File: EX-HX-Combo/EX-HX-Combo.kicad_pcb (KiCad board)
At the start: 2 copper layers, 124.5 x 120.4 mm, 46 parts, among them CN1 DB9 Male, J1 IDE_CONNECTOR, J2 Bus_Tandy_Plus, J3 Bus_Tandy_Plus_Through, SW1 SW_DIP_x10, U1 BIOS FLASH, U2 74HCT245, U3 1.8432 MHz, U4 DS1315, U5 AS6C4008-55PCN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

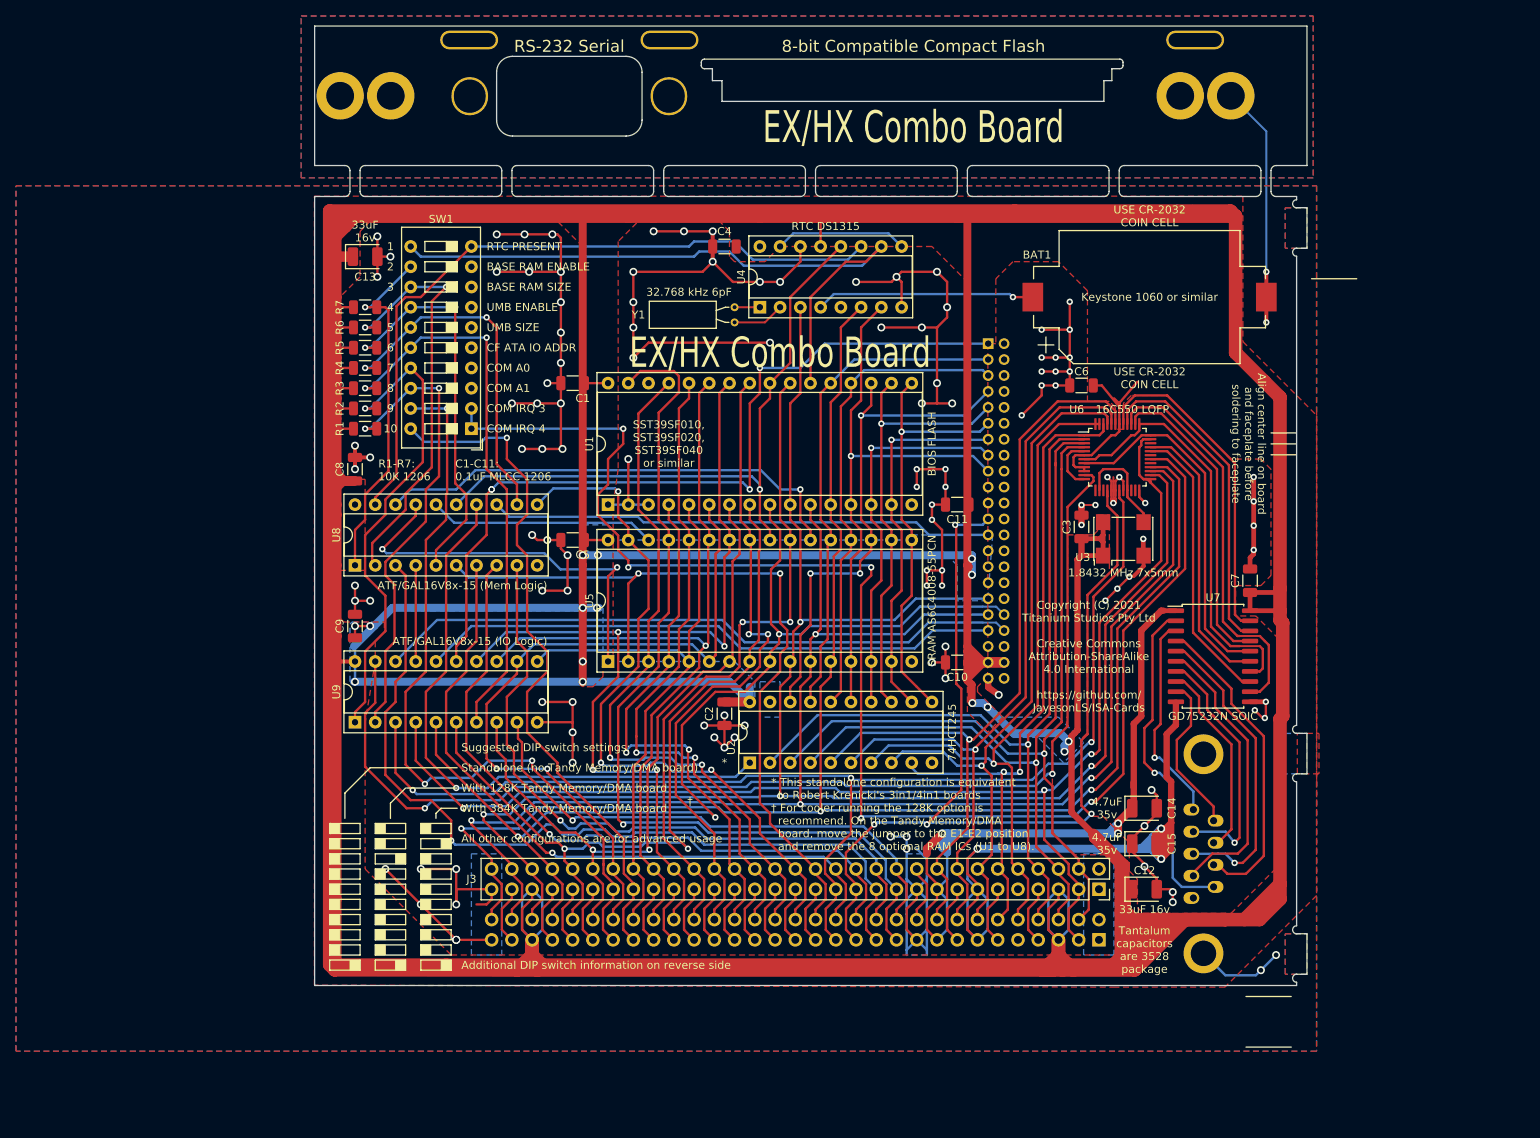
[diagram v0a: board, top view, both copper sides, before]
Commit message: EX-HX-Combo: Move backplate back to original position in prep for moving to new scene.
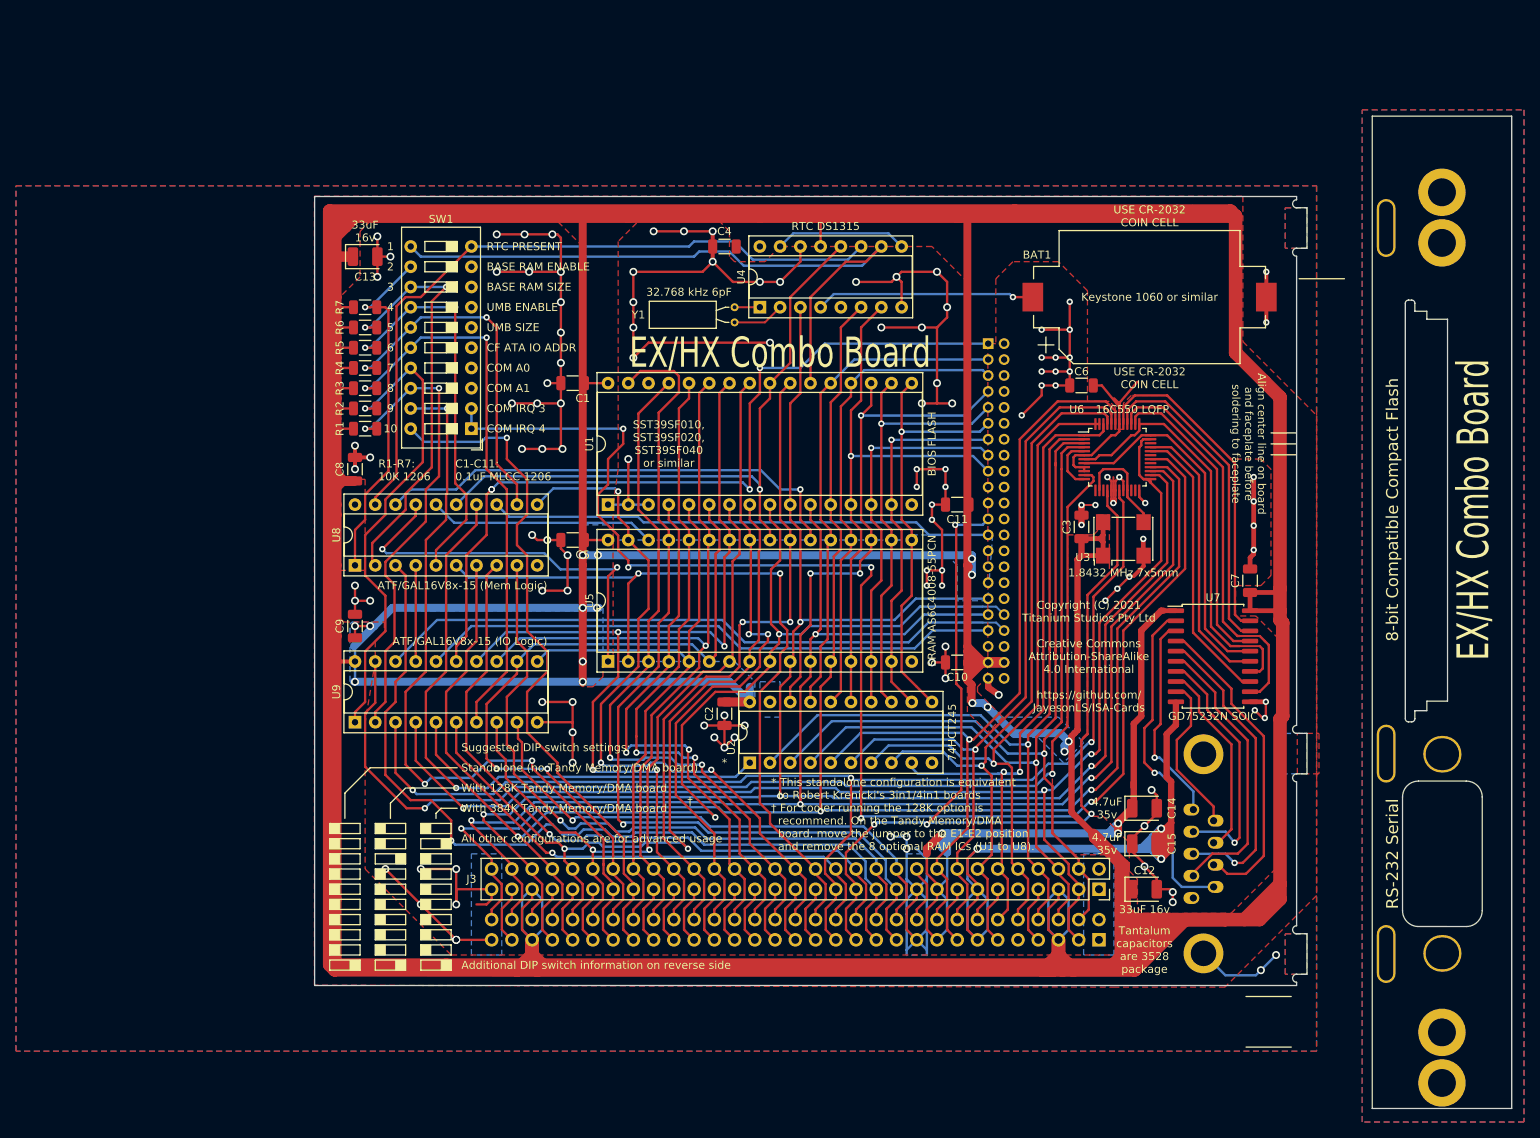
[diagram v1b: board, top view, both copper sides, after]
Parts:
- moved H4 185.6 mm to (261.5, 148.8), turned to 0 degrees
- moved H3 176.7 mm to (261.5, 142.4), turned to 0 degrees
- moved H5 162.5 mm to (254.5, 132.6), turned to 90 degrees
- moved H8 144.7 mm to (255.3, 120.0), turned to 270 degrees
- moved H6 126.9 mm to (254.5, 107.4), turned to 90 degrees
- moved H2 37.7 mm to (261.5, 43.4), turned to 0 degrees
- moved H7 33.6 mm to (254.5, 41.5), turned to 90 degrees
- moved H1 29.1 mm to (261.5, 37.0), turned to 0 degrees
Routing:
- net GND: track 497.0 -> 473.1 mm
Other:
- board size 124.5 x 120.4 mm -> 150.2 x 124.5 mm

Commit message: EX-HX-Combo: Initial work preparing for JLCPCB assembly. Other minor tweaks also.
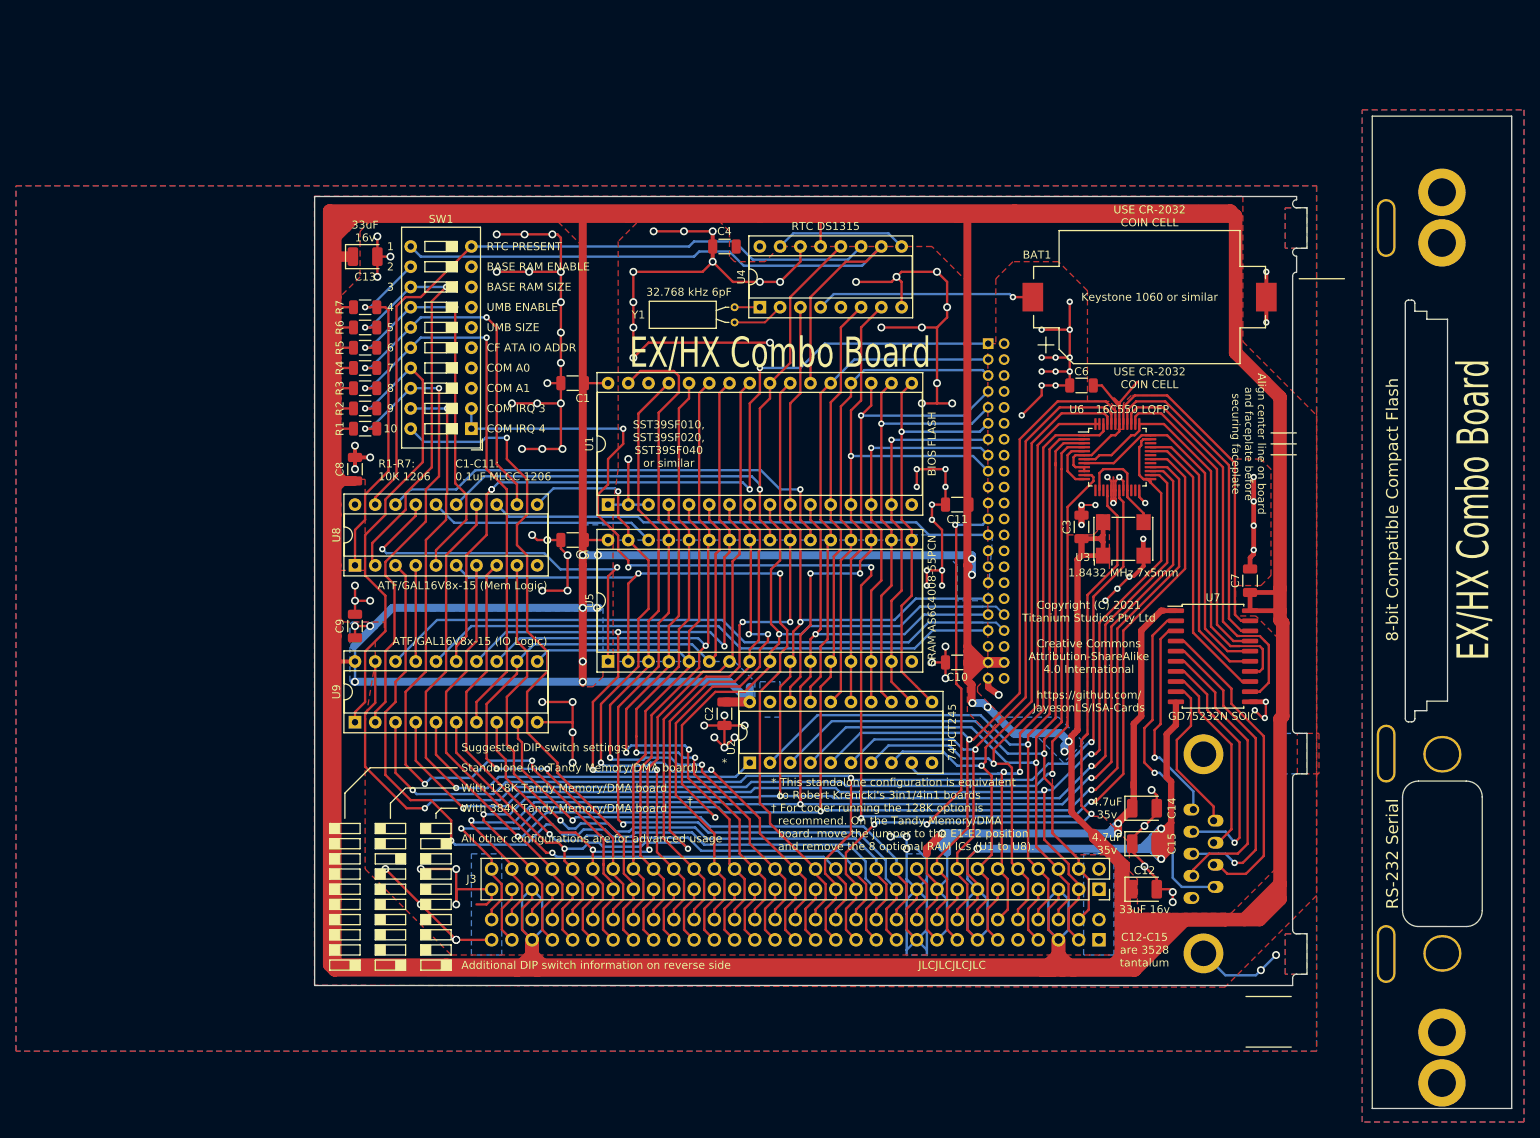
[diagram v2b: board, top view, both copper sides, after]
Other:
- outline, holes or cut-outs redrawn
- board text added: "Align center line on board and faceplate before securing faceplate"
- board text added: "C12-C15 are 3528 tantalum"
- board text added: "COM"
- board text added: "JLCJLCJLCJLC"
- board text added: "v1.01"
- board text removed: "Align center line on board and faceplate before soldering to faceplate"
- board text removed: "Serial"
- board text removed: "Tantalum capacitors are 3528 package"
- board text removed: "v1.0"

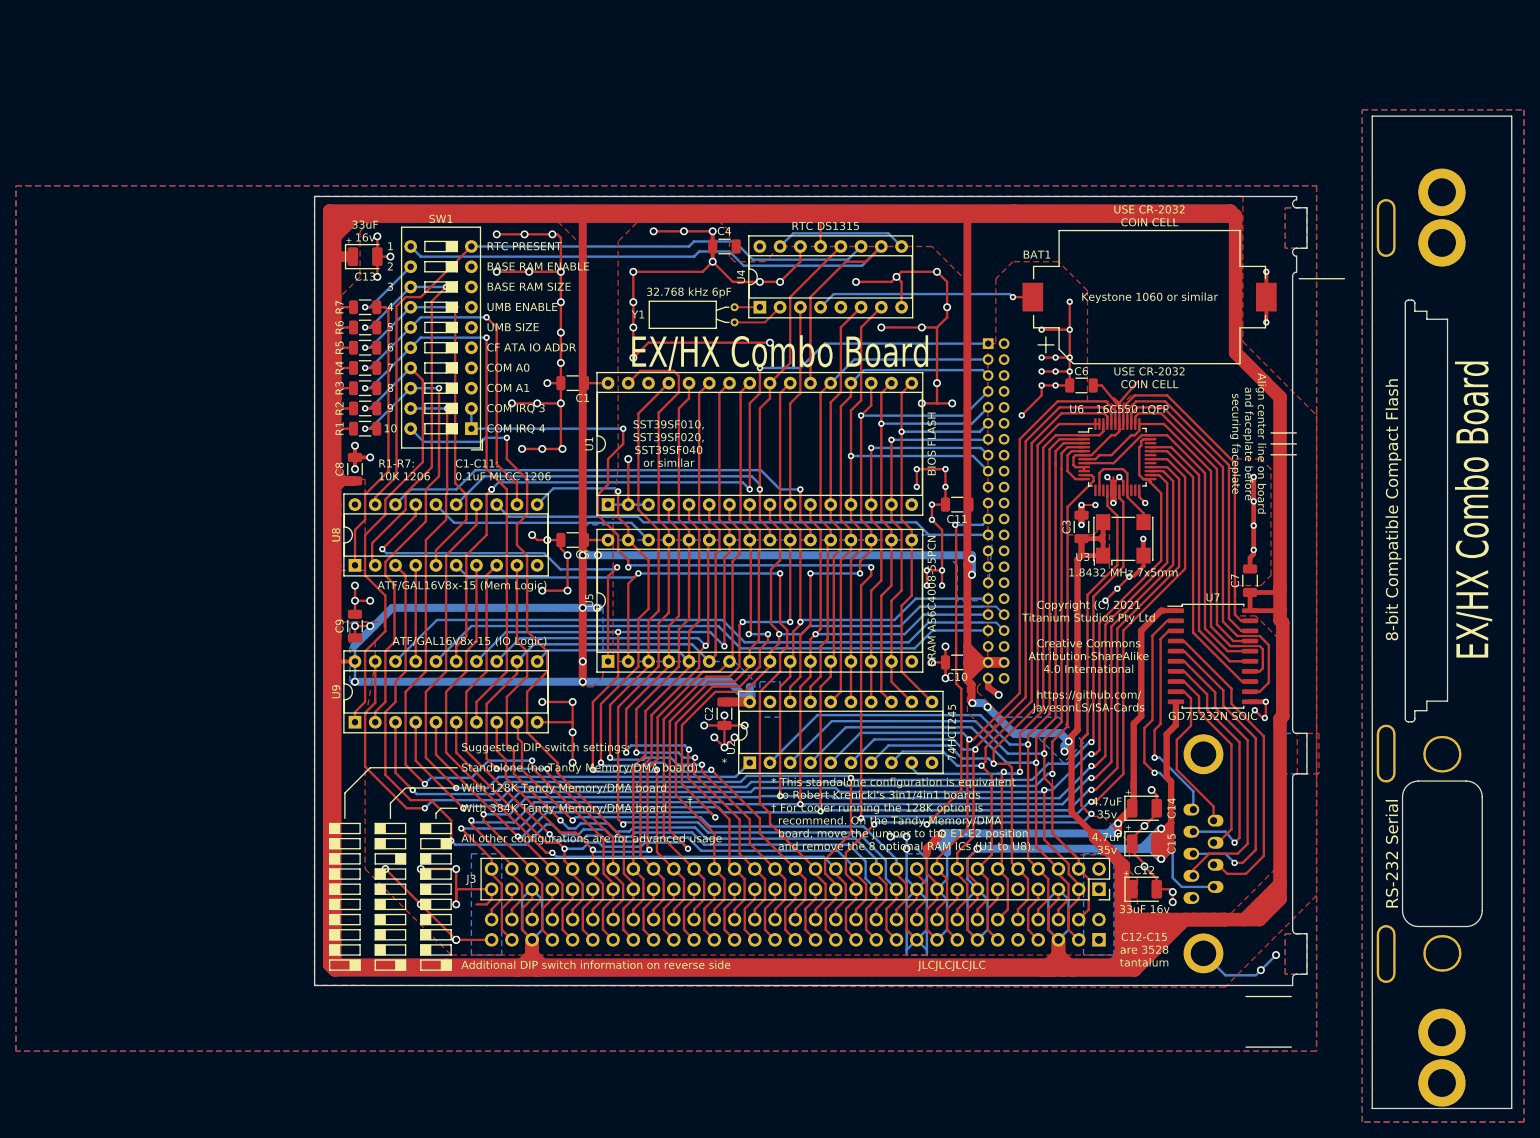
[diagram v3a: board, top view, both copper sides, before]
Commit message: Use correct DB-9 footprint on EX-HX-Combo. Also remove ground from alighment pins and space out the resitors in the top left bank.
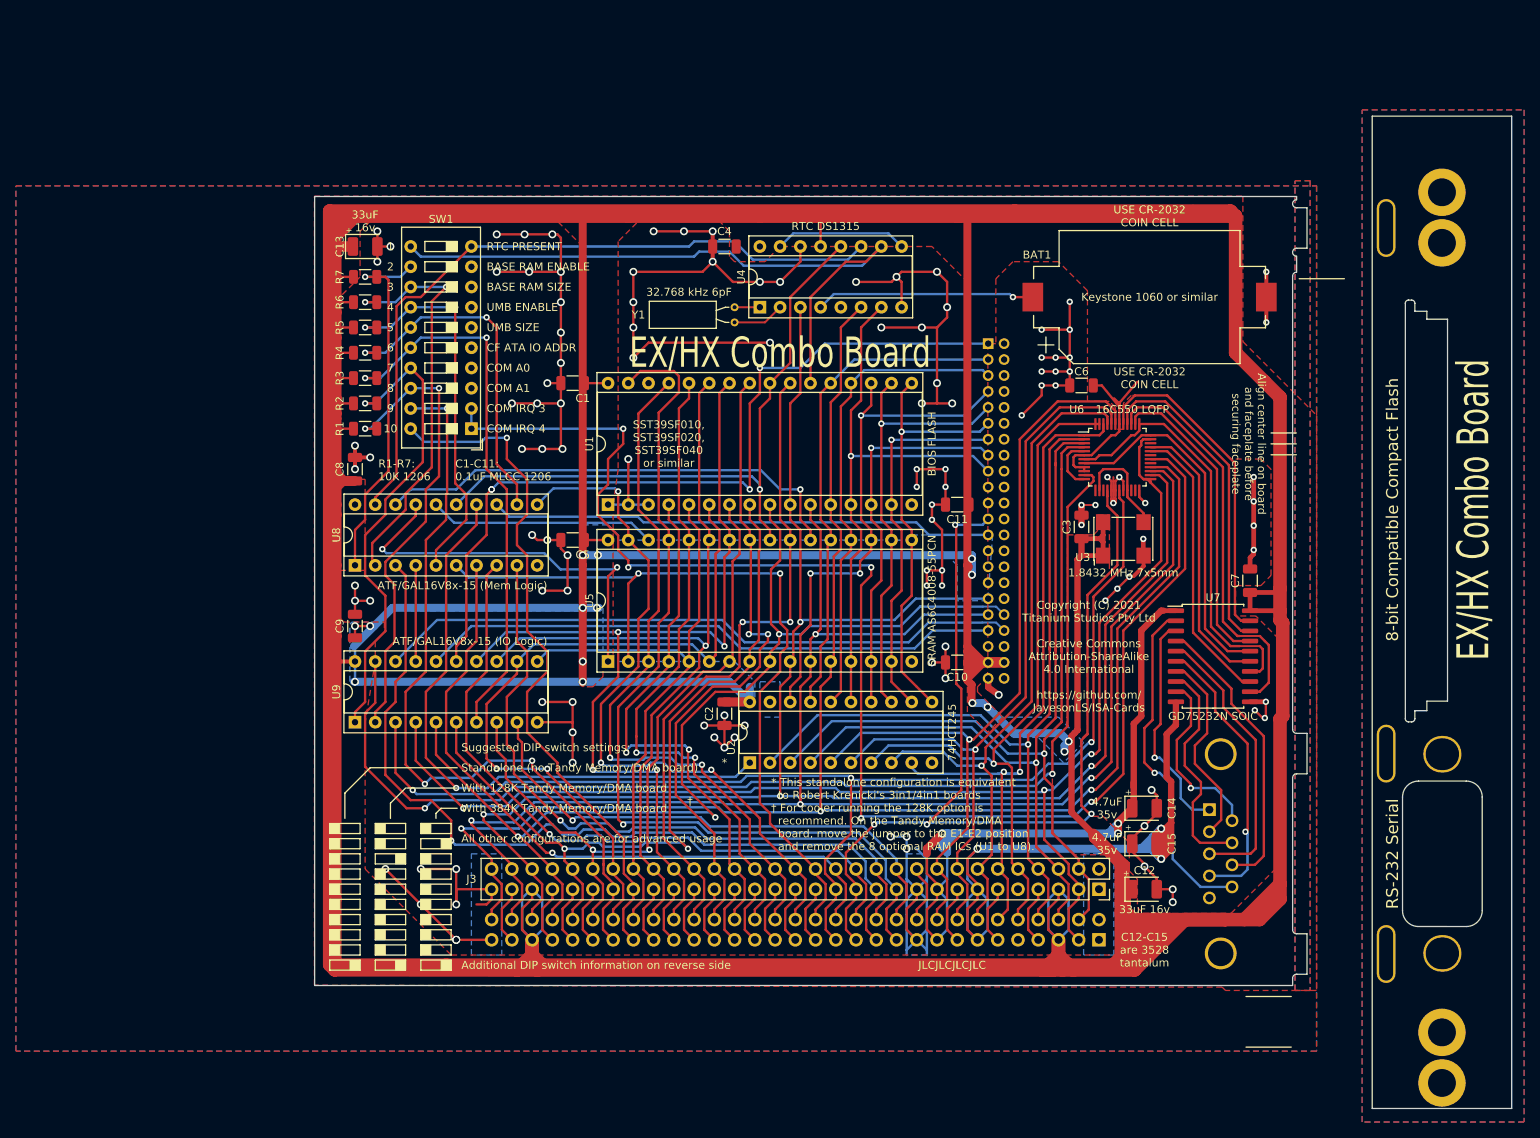
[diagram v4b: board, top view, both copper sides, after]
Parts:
- CN1: footprint w_conn_d-sub:DB_9M -> Connector_Dsub:DSUB-9_Male_Horizontal_P2.77x2.84mm_EdgePinOffset7.70mm_Housed_MountingHolesOffset9.12mm
- moved CN1 8.44 mm to (232.3, 114.5)
- moved R7 3.81 mm to (126.4, 47.6)
- moved R6 3.18 mm to (126.4, 50.8)
- moved R5 2.54 mm to (126.4, 54.0)
- moved R4 1.91 mm to (126.4, 57.1)
- moved C13 1.27 mm to (126.4, 43.8)
- moved R3 1.27 mm to (126.4, 60.3)
- moved R2 0.64 mm to (126.4, 63.5)
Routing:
- net GND: track 473.1 -> 460.5 mm, vias 124 -> 122
- net /SER_PIN2: track 31.7 -> 25.0 mm, vias 1 -> 0
- net /SER_PIN7: track 25.0 -> 28.4 mm
- net /SER_PIN8: track 39.8 -> 36.6 mm
- net /SER_PIN3: track 38.7 -> 35.6 mm, vias 1 -> 0
- net /SER_PIN6: track 20.2 -> 23.0 mm, vias 0 -> 1
- net BASE_RAM_ENABLE: track 44.6 -> 46.9 mm
- net /SER_PIN1: track 26.5 -> 28.6 mm
- net BASE_RAM_SIZE: track 52.6 -> 51.3 mm
- net UMB_ENABLE: track 49.4 -> 48.4 mm
- net /SER_PIN9: track 42.0 -> 42.9 mm
- net VCC: track 1306.3 -> 1305.4 mm
- net UMB_SIZE: track 44.4 -> 43.6 mm
- net /SER_PIN4: track 36.3 -> 35.8 mm, vias 0 -> 1
- net ATA_ADDR_JUMPER: track 70.2 -> 69.7 mm
- added copper zone on B.Cu, net (none)
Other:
- board text added: "v1.1"
- board text removed: "v1.01"
